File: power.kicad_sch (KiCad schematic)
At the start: 36 parts, among them IC1 MP2456GJ-Z, IC2 MP2456GJ-Z, U4 AP2112K-3.3TRG1, U5 AP2112K-1.8TRG1

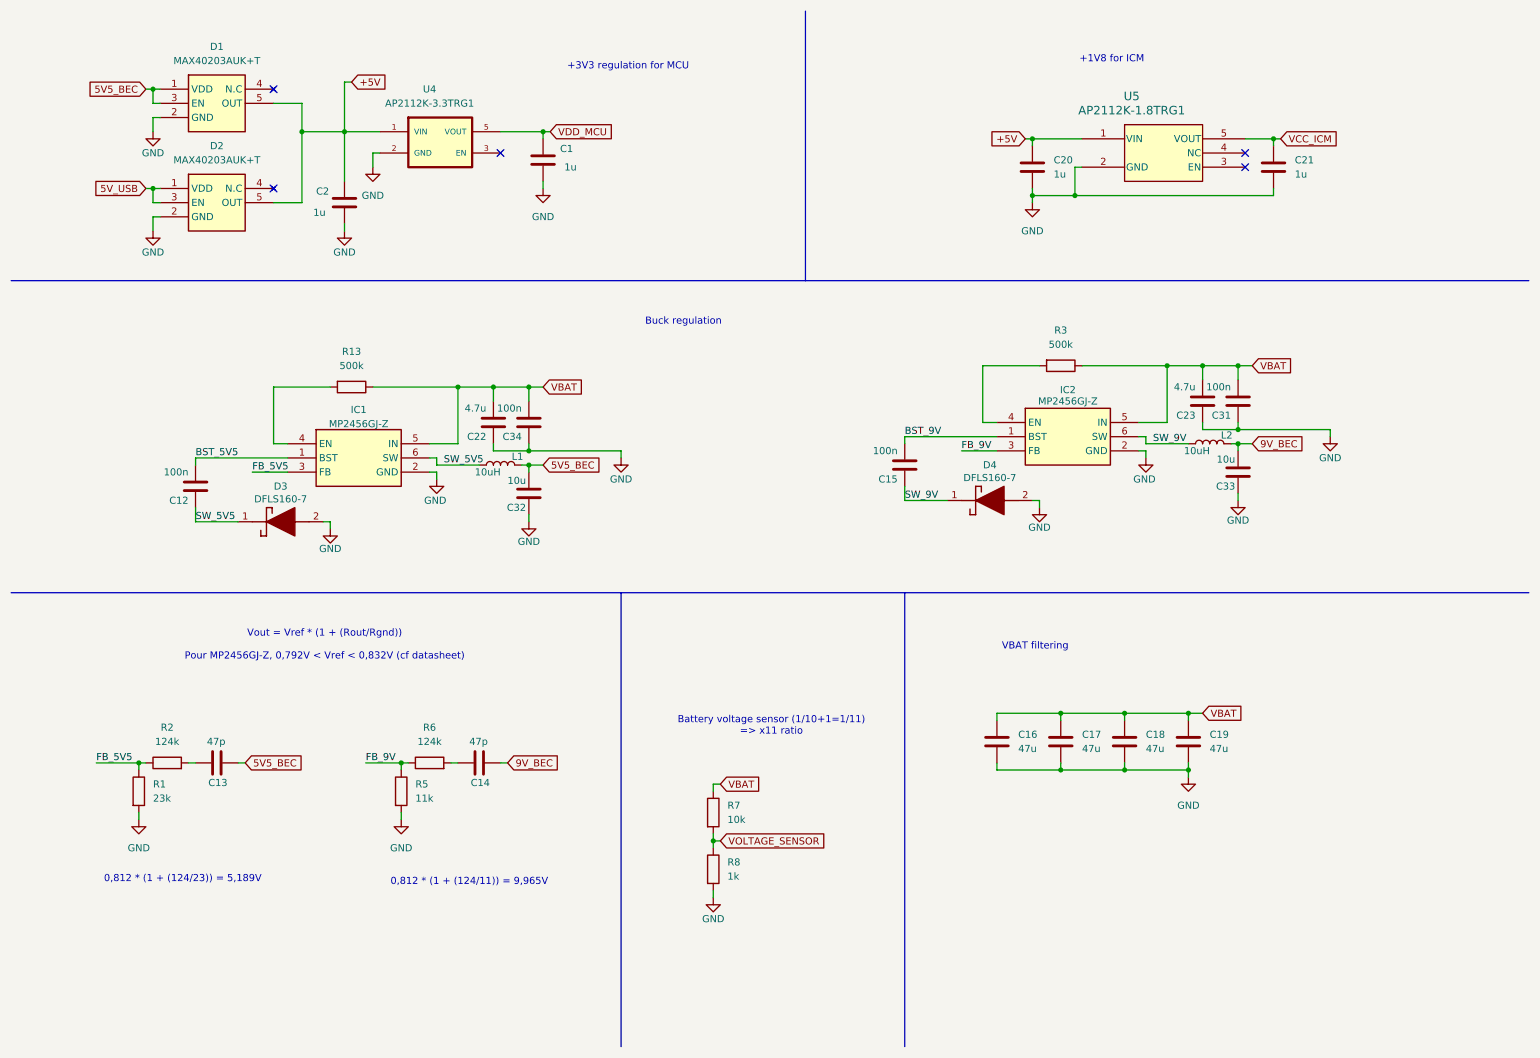
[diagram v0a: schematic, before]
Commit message: reorganized everything and switched to 0603 as a minimum size
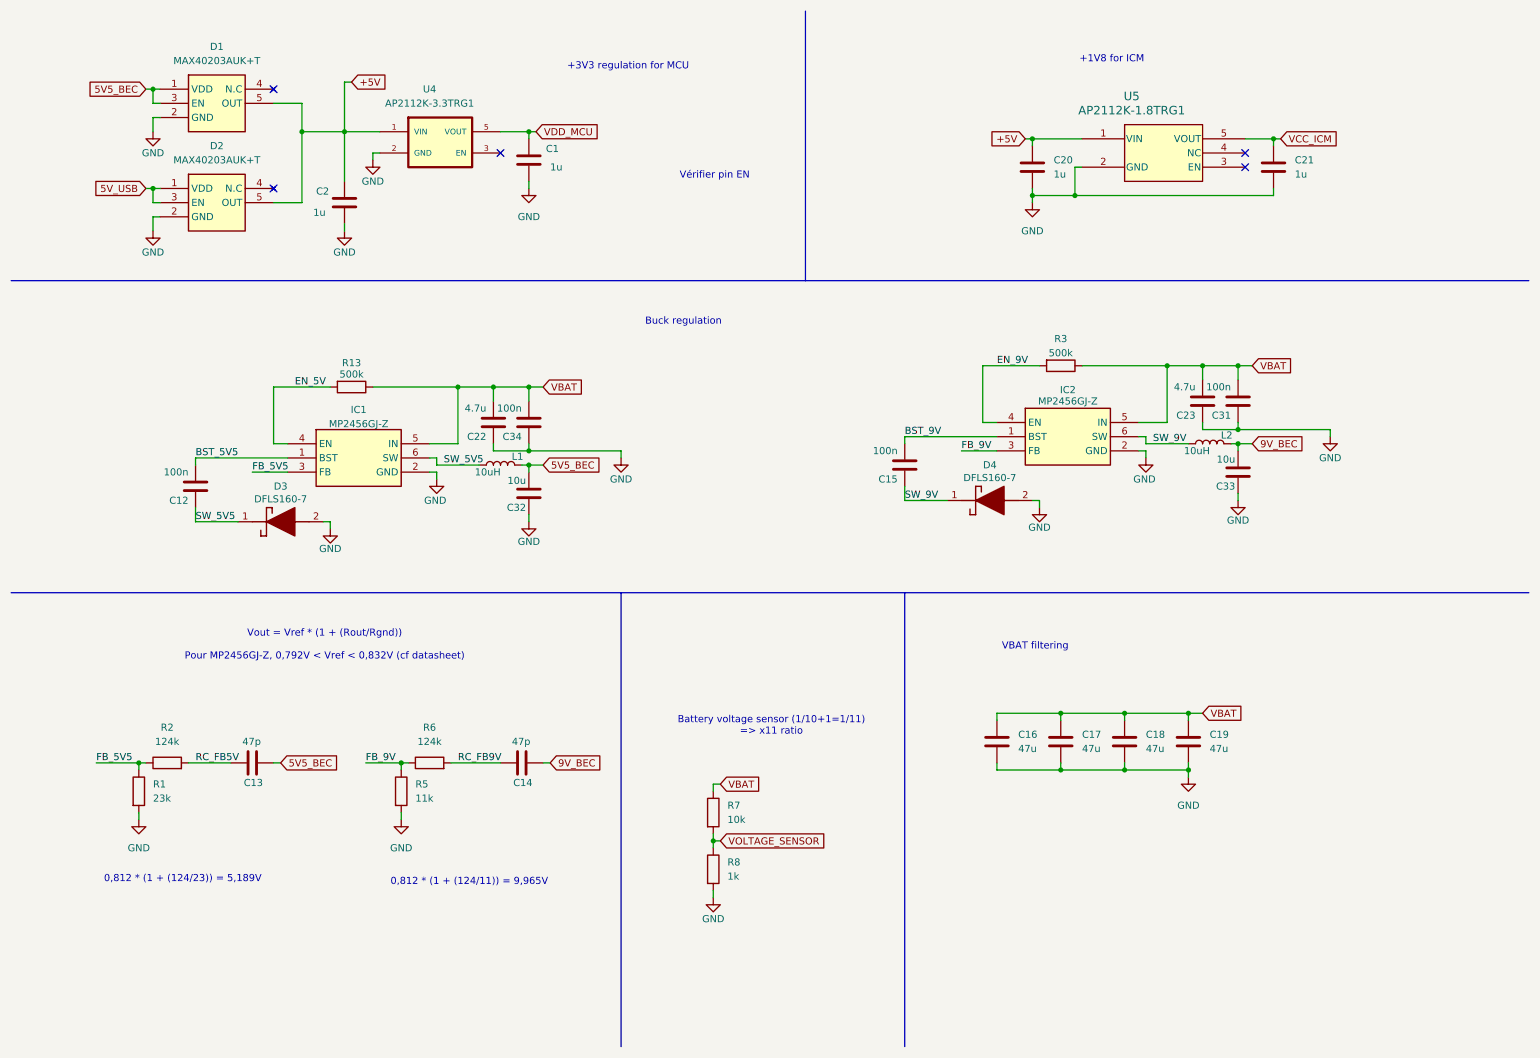
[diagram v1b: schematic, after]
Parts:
- C1, C12, C13, C14, C15, C2, C20, C21, C22, C23, C31, C34: footprint Capacitor_SMD:C_0402_1005Metric -> Capacitor_SMD:C_0603_1608Metric
- R1, R13, R2, R3, R5, R6, R7, R8: footprint Resistor_SMD:R_0402_1005Metric -> Resistor_SMD:R_0603_1608Metric
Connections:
- net EN_9V: now reaches IC2.4 (EN), R3.2
- net RC_FB9V: now reaches C14.2, R6.2
- net RC_FB5V: now reaches C13.2, R2.2
- net EN_5V: now reaches IC1.4 (EN), R13.2
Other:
- note added: "Vérifier pin EN"
- moved on the sheet: C1, C13, C14

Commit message: changed barometer to BMP580 and completed BOM
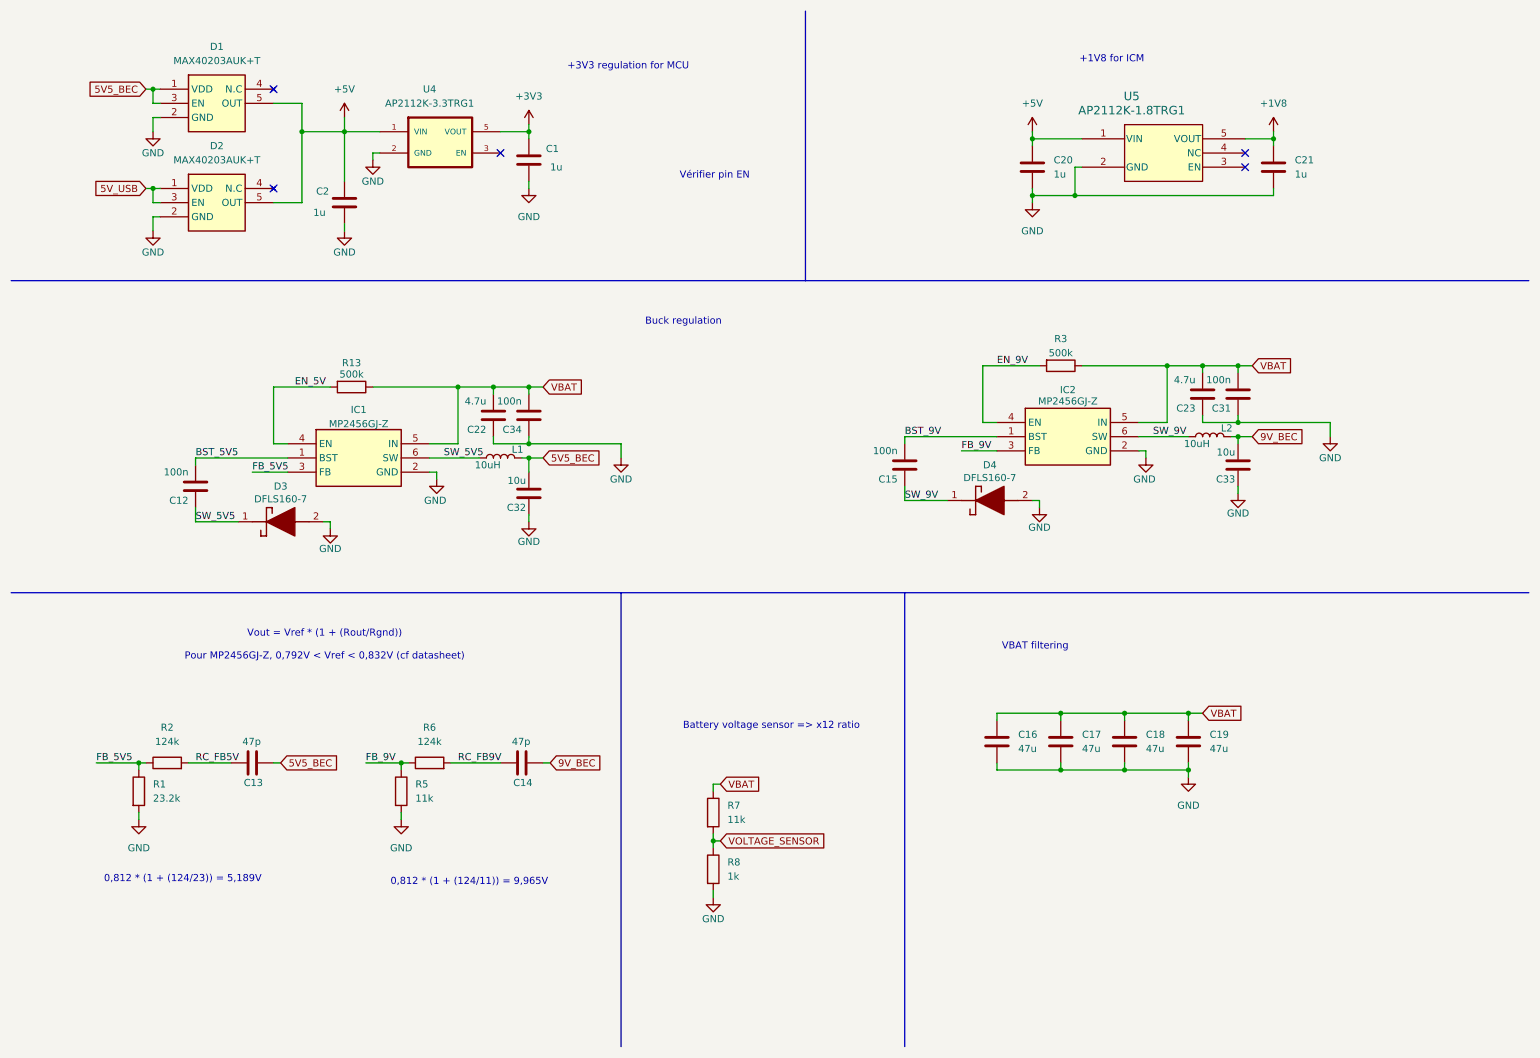
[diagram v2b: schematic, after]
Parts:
- C1, C2, C20, C21: LCSC Part Name C1518208 -> C5199872; Manufacturer_Name muRata -> Samsung Electro-Mechanics; Manufacturer_Part_Number GRM155R61H105KE05D -> CL10B105KB8NQNC
- C12, C15, C31, C34: LCSC Part Name C194427 -> C1591; Manufacturer_Name muRata -> Samsung Electro-Mechanics; Manufacturer_Part_Number GRM188R6YA106MA73D -> CL10B104KB8NNNC
- C13, C14: LCSC Part Name C29519229 -> C105622; Manufacturer_Name muRata -> YAGEO; Manufacturer_Part_Number GRM188C61E226ME01D -> CC0603JRNPO9BN470
- C16, C17, C18, C19: LCSC Part Name C403725 -> C76659; Manufacturer_Name muRata -> TDK; Manufacturer_Part_Number GRM31CR61E476ME44L -> C3216X5R1E476MTJ00E
- C22, C23: LCSC Part Name C194427 -> C307467; Manufacturer_Name muRata -> Samsung Electro-Mechanics; Manufacturer_Part_Number GRM188R6YA106MA73D -> CL10A475KL8NRNC
- C32, C33: LCSC Part Name C29519229 -> C194427; Manufacturer_Part_Number GRM188C61E226ME01D -> GRM188R6YA106MA73D
- D3, D4: LCSC Part Name (none) -> C177023
- IC1, IC2: LCSC Part Name (none) -> C49375217
- R1: value 23k -> 23.2k; LCSC Part Name C155695 -> C861768; Manufacturer_Part_Number RC0402FR-077K68L -> RT0603BRE0723K2L
- R13, R3: LCSC Part Name C138033 -> C26751; Manufacturer_Name YAGEO -> UNI-ROYAL; Manufacturer_Part_Number RC0402FR-071ML -> 0603WAF4993T5E
- R2, R6: LCSC Part Name C26978 -> C22788; Manufacturer_Part_Number 0402WGF4122TCE -> 0603WAF1243T5E
- R5: LCSC Part Name C137988 -> C25950; Manufacturer_Name YAGEO -> UNI-ROYAL; Manufacturer_Part_Number RC0402FR-073K92L -> 0603WAF1102T5E
- R7: value 10k -> 11k; LCSC Part Name C60490 -> C25950; Manufacturer_Name YAGEO -> UNI-ROYAL; Manufacturer_Part_Number RC0402FR-0710KL -> 0603WAF1102T5E
- R8: LCSC Part Name C106235 -> C22548; Manufacturer_Part_Number RC0402FR-071KL -> RC0603FR-071KL
- U4: LCSC Part Name (none) -> C51118
- U5: LCSC Part Name (none) -> C176944
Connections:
- net VCC_ICM renamed +1V8
- net VDD_MCU renamed +3V3
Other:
- note added: "Battery voltage sensor => x12 ratio"
- note removed: "Battery voltage sensor (1/10+1=1/11) => x11 ratio"
- moved on the sheet: C22, C23, C31, C33, C34, L1, L2

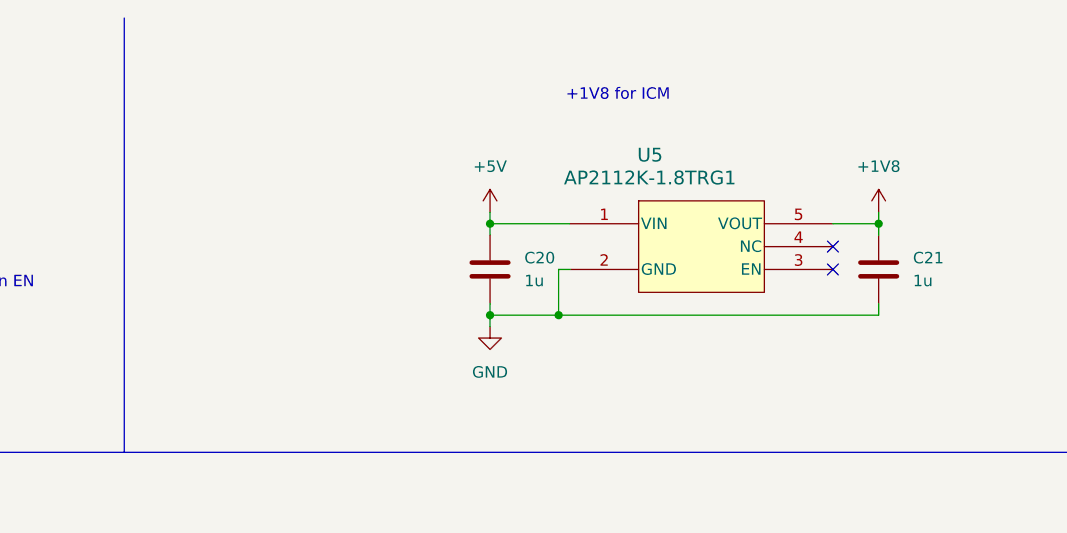
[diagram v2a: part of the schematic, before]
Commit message: switch IMU to BMI270
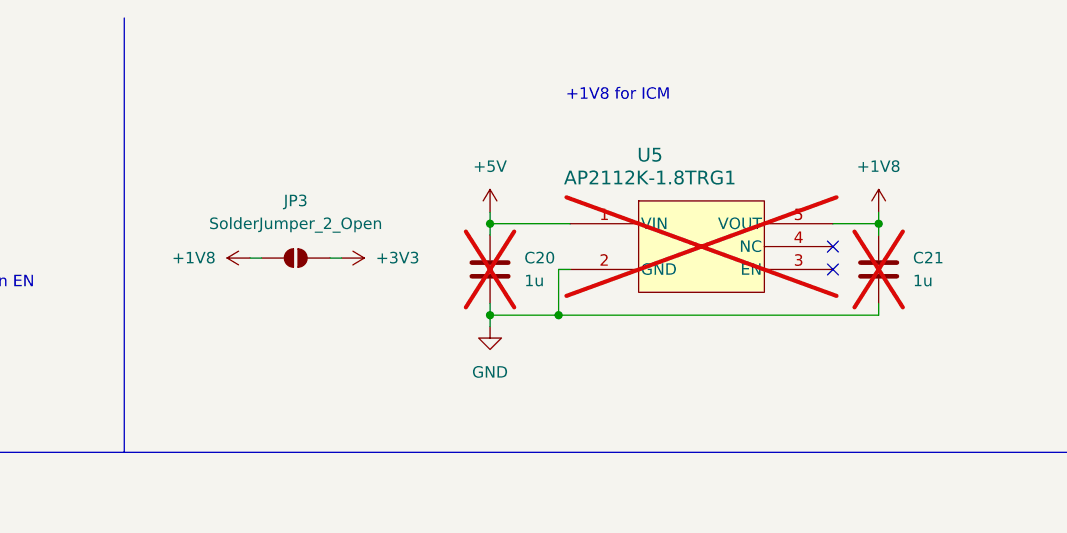
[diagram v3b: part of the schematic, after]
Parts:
- added JP3: SolderJumper_2_Open, Jumper:SolderJumper-2_P1.3mm_Open_TrianglePad1.0x1.5mm, symbol Jumper:SolderJumper_2_Open
- C20, C21: now not fitted
- U5: now not fitted; now left out of the parts list
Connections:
- net +1V8: now also JP3.1 (A)
- net +3V3: now also JP3.2 (B)
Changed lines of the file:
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@@
 	(wire
 		(pts
+			(xy 177.8 39.37) (xy 179.07 39.37)
+		)
+		(stroke
+			(width 0)
+			(type default)
+		)
+	)
+	(wire
+		(pts
 			(xy 231.14 88.9) (xy 232.41 88.9)
 		)
@@
 	(wire
 		(pts
+			(xy 168.91 39.37) (xy 170.18 39.37)
+		)
+		(stroke
+			(width 0)
+			(type default)
+		)
+	)
+	(wire
+		(pts
 			(xy 138.43 151.13) (xy 138.43 152.4)
 		)
@@
 	)
 	(symbol
+		(lib_id "power:+1V8")
+		(at 168.91 39.37 90)
+		(unit 1)
+		(exclude_from_sim no)
+		(in_bom yes)
+		(on_board yes)
+		(dnp no)
+		(fields_autoplaced yes)
+		(property "Reference" "#PWR019"
+			(at 172.72 39.37 0)
+			(effects
+				(font
+					(size 1.27 1.27)
+				)
+				(hide yes)
+			)
+		)
+		(property "Value" "+1V8"
+			(at 165.1 39.3699 90)
+			(effects
+				(font
+					(size 1.27 1.27)
+				)
+				(justify left)
+			)
+		)
+		(property "Footprint" ""
+			(at 168.91 39.37 0)
+			(effects
+				(font
+					(size 1.27 1.27)
+				)
+				(hide yes)
+			)
+		)
+		(property "Datasheet" ""
+			(at 168.91 39.37 0)
+			(effects
+				(font
+					(size 1.27 1.27)
+				)
+				(hide yes)
+			)
+		)
+		(property "Description" "Power symbol creates a global label with name \"+1V8\""
+			(at 168.91 39.37 0)
+			(effects
+				(font
+					(size 1.27 1.27)
+				)
+				(hide yes)
+			)
+		)
+		(pin "1"
+		)
+		(instances
+			(project "fcg4"
+				(path "/ebe93c2f-0aae-4f69-99fc-930f63b0ac94/1e919846-8db7-427a-a45e-eaa9fec3e7ae"
+					(reference "#PWR019")
+					(unit 1)
+				)
+			)
+		)
+	)
+	(symbol
 		(lib_id "power:GND")
 		(at 195.58 46.99 0)
@@
 		(unit 1)
 		(exclude_from_sim no)
-		(in_bom yes)
+		(in_bom no)
 		(on_board yes)
-		(dnp no)
+		(dnp yes)
 		(fields_autoplaced yes)
 		(property "Reference" "U5"
@@
 		(in_bom yes)
 		(on_board yes)
-		(dnp no)
+		(dnp yes)
 		(fields_autoplaced yes)
 		(property "Reference" "C20"
@@
 	)
 	(symbol
+		(lib_id "Jumper:SolderJumper_2_Open")
+		(at 173.99 39.37 0)
+		(unit 1)
+		(exclude_from_sim no)
+		(in_bom no)
+		(on_board yes)
+		(dnp no)
+		(fields_autoplaced yes)
+		(property "Reference" "JP3"
+			(at 173.99 33.02 0)
+			(effects
+				(font
+					(size 1.27 1.27)
+				)
+			)
+		)
+		(property "Value" "SolderJumper_2_Open"
+			(at 173.99 35.56 0)
+			(effects
+				(font
+					(size 1.27 1.27)
+				)
+			)
+		)
+		(property "Footprint" "Jumper:SolderJumper-2_P1.3mm_Open_TrianglePad1.0x1.5mm"
+			(at 173.99 39.37 0)
+			(effects
+				(font
+					(size 1.27 1.27)
+				)
+				(hide yes)
+			)
+		)
+		(property "Datasheet" "~"
+			(at 173.99 39.37 0)
+			(effects
+				(font
+					(size 1.27 1.27)
+				)
+				(hide yes)
+			)
+		)
+		(property "Description" "Solder Jumper, 2-pole, open"
+			(at 173.99 39.37 0)
+			(effects
+				(font
+					(size 1.27 1.27)
+				)
+				(hide yes)
+			)
+		)
+		(pin "2"
+		)
+		(pin "1"
+		)
+		(instances
+			(project "fcg4"
+				(path "/ebe93c2f-0aae-4f69-99fc-930f63b0ac94/1e919846-8db7-427a-a45e-eaa9fec3e7ae"
+					(reference "JP3")
+					(unit 1)
+				)
+			)
+		)
+	)
+	(symbol
 		(lib_id "power:GND")
 		(at 69.85 105.41 0)
@@
 	)
 	(symbol
+		(lib_id "power:+3V3")
+		(at 179.07 39.37 270)
+		(unit 1)
+		(exclude_from_sim no)
+		(in_bom yes)
+		(on_board yes)
+		(dnp no)
+		(fields_autoplaced yes)
+		(property "Reference" "#PWR020"
+			(at 175.26 39.37 0)
+			(effects
+				(font
+					(size 1.27 1.27)
+				)
+				(hide yes)
+			)
+		)
+		(property "Value" "+3V3"
+			(at 182.88 39.3699 90)
+			(effects
+				(font
+					(size 1.27 1.27)
+				)
+				(justify left)
+			)
+		)
+		(property "Footprint" ""
+			(at 179.07 39.37 0)
+			(effects
+				(font
+					(size 1.27 1.27)
+				)
+				(hide yes)
+			)
+		)
+		(property "Datasheet" ""
+			(at 179.07 39.37 0)
+			(effects
+				(font
+					(size 1.27 1.27)
+				)
+				(hide yes)
+			)
+		)
+		(property "Description" "Power symbol creates a global label with name \"+3V3\""
+			(at 179.07 39.37 0)
+			(effects
+				(font
+					(size 1.27 1.27)
+				)
+				(hide yes)
+			)
+		)
+		(pin "1"
+		)
+		(instances
+			(project "fcg4"
+				(path "/ebe93c2f-0aae-4f69-99fc-930f63b0ac94/1e919846-8db7-427a-a45e-eaa9fec3e7ae"
+					(reference "#PWR020")
+					(unit 1)
+				)
+			)
+		)
+	)
+	(symbol
 		(lib_id "Device:L")
 		(at 227.33 88.9 90)
@@
 		(in_bom yes)
 		(on_board yes)
-		(dnp no)
+		(dnp yes)
 		(fields_autoplaced yes)
 		(property "Reference" "C21"
